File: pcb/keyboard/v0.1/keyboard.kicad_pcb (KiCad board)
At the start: 4 copper layers, 80 x 51 mm, 123 parts, among them J1 USB2.0, J2 SWD, SW1 TAB, SW10 O, SW11 P, SW12 RETURN, SW13 CAPS, SW14 A, SW15 S, SW16 D, SW17 F, SW18 G, SW19 H, SW2 Q, SW20 J, SW21 K, SW22 L, SW23 SEMI, SW24 QUOTE, SW25 LSHIFT, SW26 Z, SW27 X, SW28 C, SW29 V, SW3 W, SW30 B, SW31 N, SW32 M, SW33 COMMA, SW34 DOT, SW35 QUEST, SW36 RSHIFT, SW37 FN, SW38 LCTRL, SW39 LSUPER, SW4 E, SW40 LALT, SW41 SPACE, SW42 SPACE, SW43 RALT, SW44 RSUPER, SW45 C8, SW46 RCTRL, SW47 C1, SW48 C2, SW49 C3, SW5 R, SW50 C4, SW51 C5, SW52 C6, SW53 C7, SW6 T, SW7 Y, SW8 U, SW9 I, U1 MDBT50Q-P1MV2, Y1 32.768

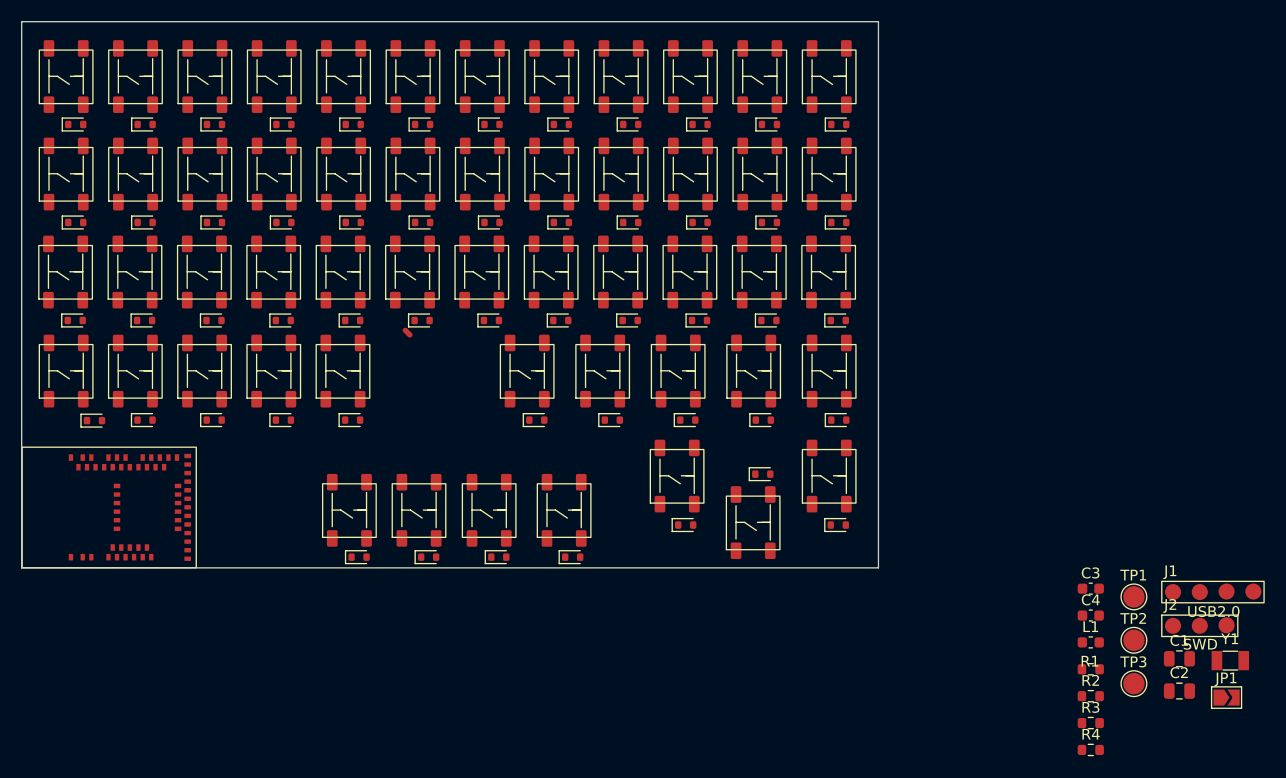
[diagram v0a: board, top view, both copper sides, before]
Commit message: Basic power circuitry done
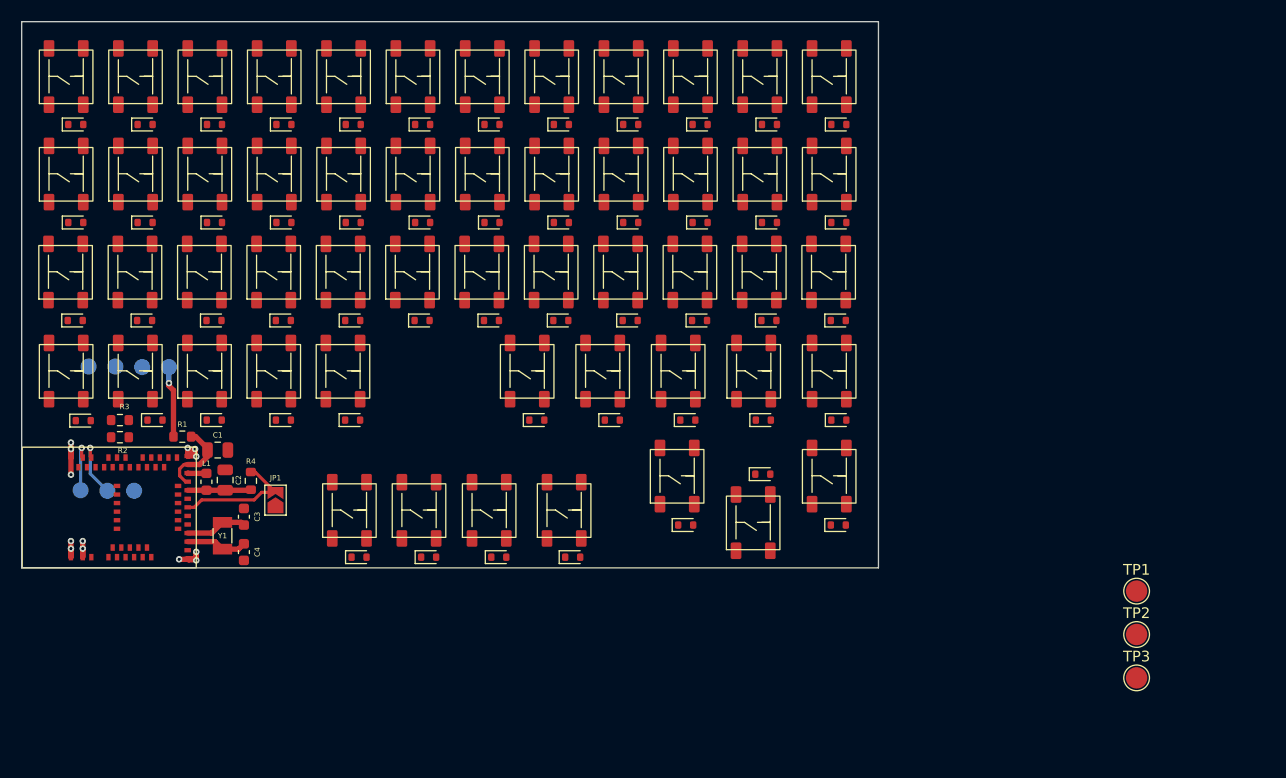
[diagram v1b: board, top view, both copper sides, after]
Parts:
- J1, J2: moved to B.Cu
- moved J2 97.8 mm to (35.5, 79.8), turned to 180 degrees
- moved J1 96.1 mm to (38.8, 68.2), turned to 180 degrees
- moved R3 95.0 mm to (34.2, 73.2), turned to 180 degrees
- moved Y1 94.8 mm to (43.8, 84.0), turned to -90 degrees
- moved R2 93.8 mm to (34.2, 74.8)
- moved C1 91.9 mm to (43.3, 76.0)
- moved C2 91.3 mm to (44.0, 78.8), turned to 90 degrees
- moved JP1 90.7 mm to (48.7, 80.7), turned to 90 degrees
- moved R1 87.6 mm to (40.0, 74.8)
- moved L1 83.9 mm to (42.2, 79.0), turned to -90 degrees
- moved R4 82.4 mm to (46.4, 78.9), turned to 90 degrees
- moved C3 79.4 mm to (45.8, 82.2), turned to -90 degrees
- moved C4 79.3 mm to (45.8, 85.5), turned to -90 degrees
- moved D37 1.05 mm to (30.8, 73.2)
- moved D38 0.94 mm to (37.5, 73.2)
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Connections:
- U1 pad 24: unconnected-(U1A-P0.08-Pad24) -> /ofeature_enable
- U1 pad 8: /ofeature_enable -> unconnected-(U1A-P1.15_LF-Pad8)
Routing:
- net GND: track 0.00 -> 16.2 mm, vias 0 -> 13
- net /ofeature_enable: track 0.00 -> 11.9 mm
- net /VBUS: track 0.00 -> 7.45 mm
- net /VBUS_USB: track 0.00 -> 6.68 mm, vias 0 -> 1
- net VDD: track 0.00 -> 5.92 mm
- net /XL2: track 0.00 -> 5.77 mm
- net /XL1: track 0.00 -> 5.75 mm
- net /SWDIO: track 0.00 -> 5.60 mm, vias 0 -> 1
- net /SWDCLK: track 0.00 -> 4.93 mm, vias 0 -> 1
- net /DCCH: track 0.00 -> 1.76 mm
- net /SOURCE4: track 0.60 -> 0.00 mm
- added copper zone on In1.Cu, net GND
- added copper zone on In2.Cu, net VDD
